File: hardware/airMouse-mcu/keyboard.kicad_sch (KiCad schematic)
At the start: 36 parts, among them J1 DS1020-07-16VBT1A-R

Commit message: add mouse pcb
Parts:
- renumbered C7 to C16, C8 to C17, C9 to C18, C10 to C19, C6 to C20, C11 to C21, C12 to C22, C13 to C23, C14 to C24, C15 to C25, J1 to J4, R1 to R18, R2 to R19, R13 to R20, R14 to R21, R15 to R22, R3 to R23, R4 to R24, R5 to R25, R6 to R26, R7 to R27, R8 to R28, R9 to R29, R10 to R30, R11 to R31, R12 to R32, R16 to R33, R17 to R34, R18 to R35, R19 to R36, R20 to R37, R21 to R38, R22 to R39, R23 to R40, R24 to R41, R25 to R42

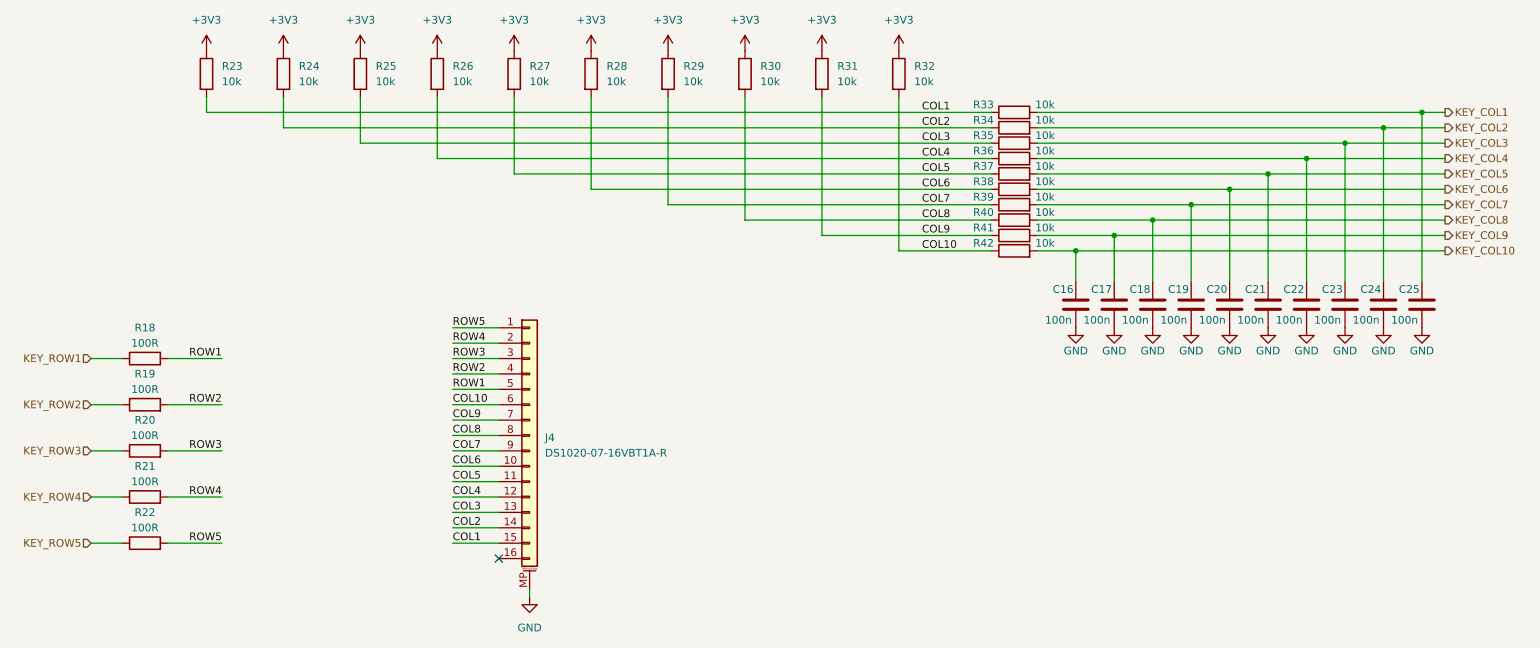
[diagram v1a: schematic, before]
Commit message: components placed on mcu board
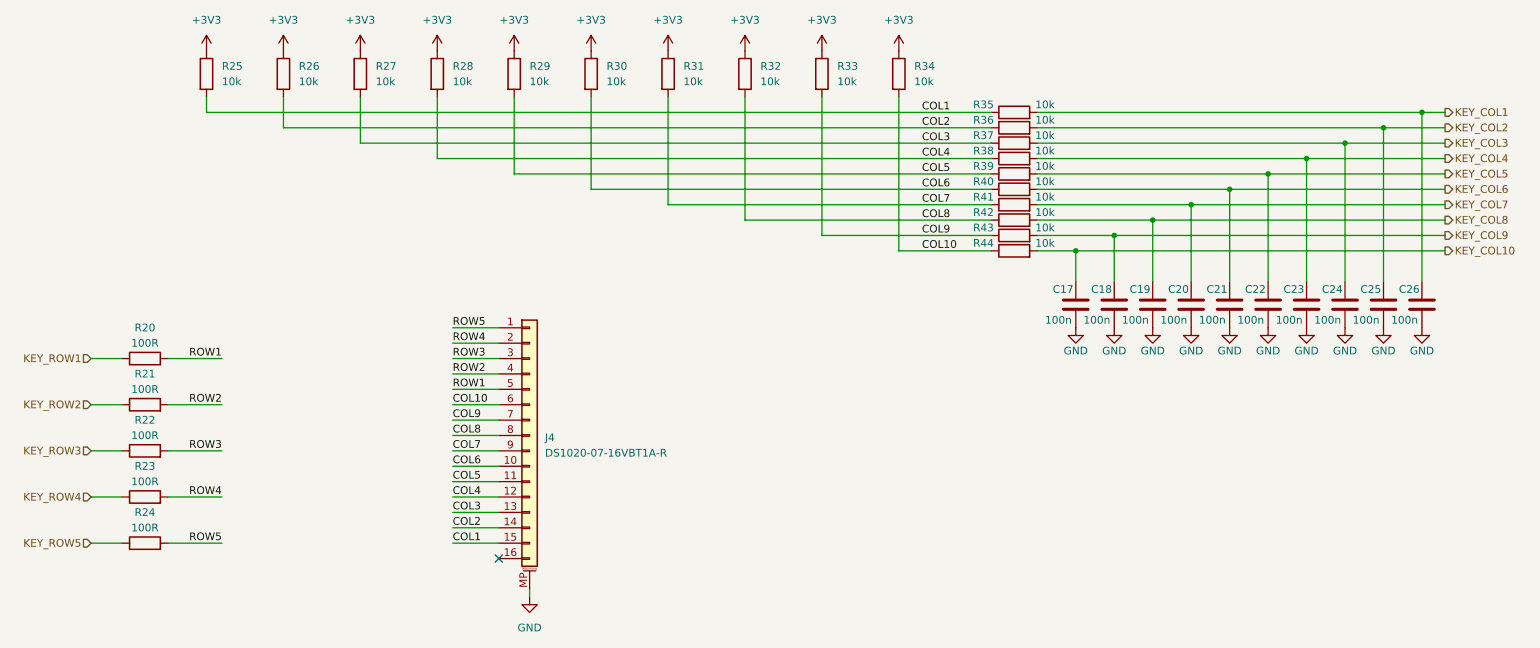
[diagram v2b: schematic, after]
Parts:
- renumbered C16 to C17, C17 to C18, C18 to C19, C19 to C20, C20 to C21, C21 to C22, C22 to C23, C23 to C24, C24 to C25, C25 to C26, R18 to R20, R19 to R21, R20 to R22, R21 to R23, R22 to R24, R23 to R25, R24 to R26, R25 to R27, R26 to R28, R27 to R29, R28 to R30, R29 to R31, R30 to R32, R31 to R33, R32 to R34, R33 to R35, R34 to R36, R35 to R37, R36 to R38, R37 to R39, R38 to R40, R39 to R41, R40 to R42, R41 to R43, R42 to R44

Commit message: add mcu board
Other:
- title: EtherPointer -> EtherPointer mcu
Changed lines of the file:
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@@
 	(paper "A4")
 	(title_block
-		(title "EtherPointer")
-		(date "2025-02-13")
+		(title "EtherPointer mcu")
+		(date "2025-02-15")
 		(rev "RC1")
 		(company "Bart's Design")

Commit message: new mcu pcb
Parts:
- removed C17, C18, C19, C20, C21, C22, C23, C24, C25, C26: 100n, Capacitor_SMD:C_0603_1608Metric, symbol Device:C
- removed R25, R26, R27, R28, R29, R30, R31, R32, R33, R34, R35, R36, R37, R38, R39, R40, R41, R42, R43, R44: 10k, Resistor_SMD:R_0603_1608Metric, symbol Device:R
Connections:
- net COL1 is gone; now on net KEY_COL1: J4.15 (Pin_15)
- net COL10 is gone; now on net KEY_COL10: J4.6 (Pin_6)
- net COL2 is gone; now on net KEY_COL2: J4.14 (Pin_14)
- net COL3 is gone; now on net KEY_COL3: J4.13 (Pin_13)
- net COL4 is gone; now on net KEY_COL4: J4.12 (Pin_12)
- net COL5 is gone; now on net KEY_COL5: J4.11 (Pin_11)
- net COL6 is gone; now on net KEY_COL6: J4.10 (Pin_10)
- net COL7 is gone; now on net KEY_COL7: J4.9 (Pin_9)
- net COL8 is gone; now on net KEY_COL8: J4.8 (Pin_8)
- net COL9 is gone; now on net KEY_COL9: J4.7 (Pin_7)

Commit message: new mcu-pcb
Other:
- title: EtherPointer mcu -> Neuro Glider
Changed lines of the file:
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@@
 	(paper "A4")
 	(title_block
-		(title "EtherPointer mcu")
-		(date "2025-02-15")
-		(rev "RC1")
+		(title "Neuro Glider")
+		(date "2025-03-21")
+		(rev "v1.0")
 		(company "Bart's Design")
 		(comment 1 "Bartosz Pracz")
